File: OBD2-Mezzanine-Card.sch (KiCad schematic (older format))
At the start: 15 parts, among them P1 CONN_02X20

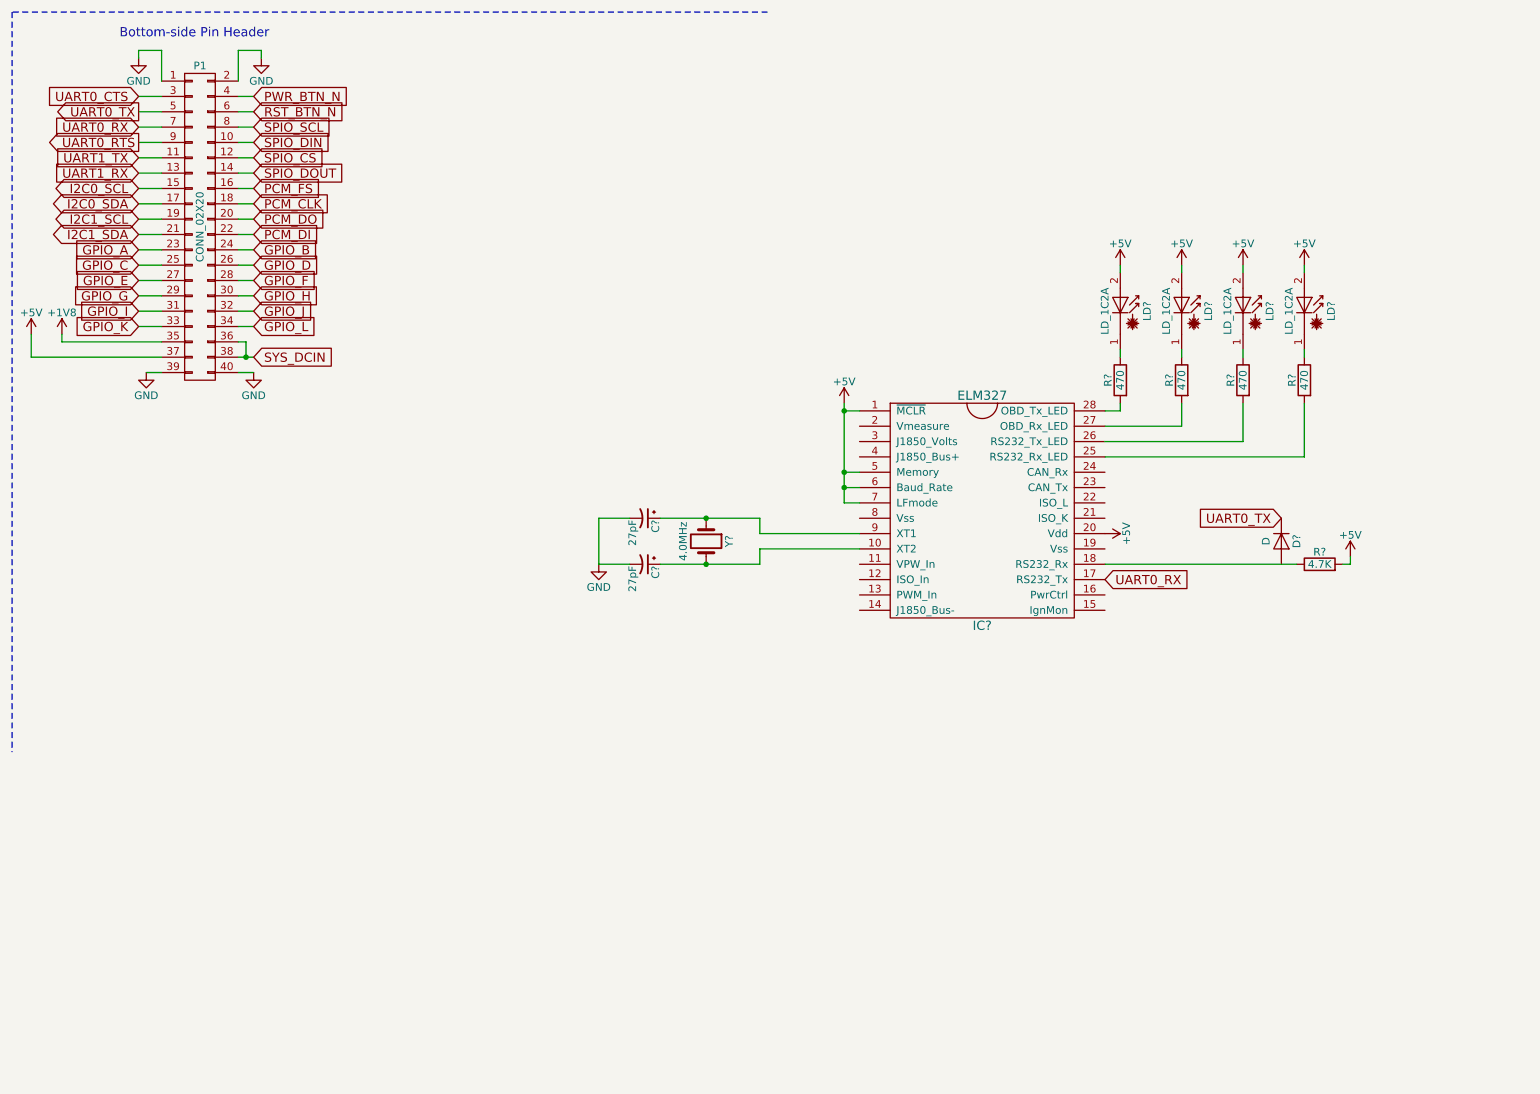
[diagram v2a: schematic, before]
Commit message: sch: Rearange
Signed-off-by: Alistair Francis <alistair@alistair23.me>
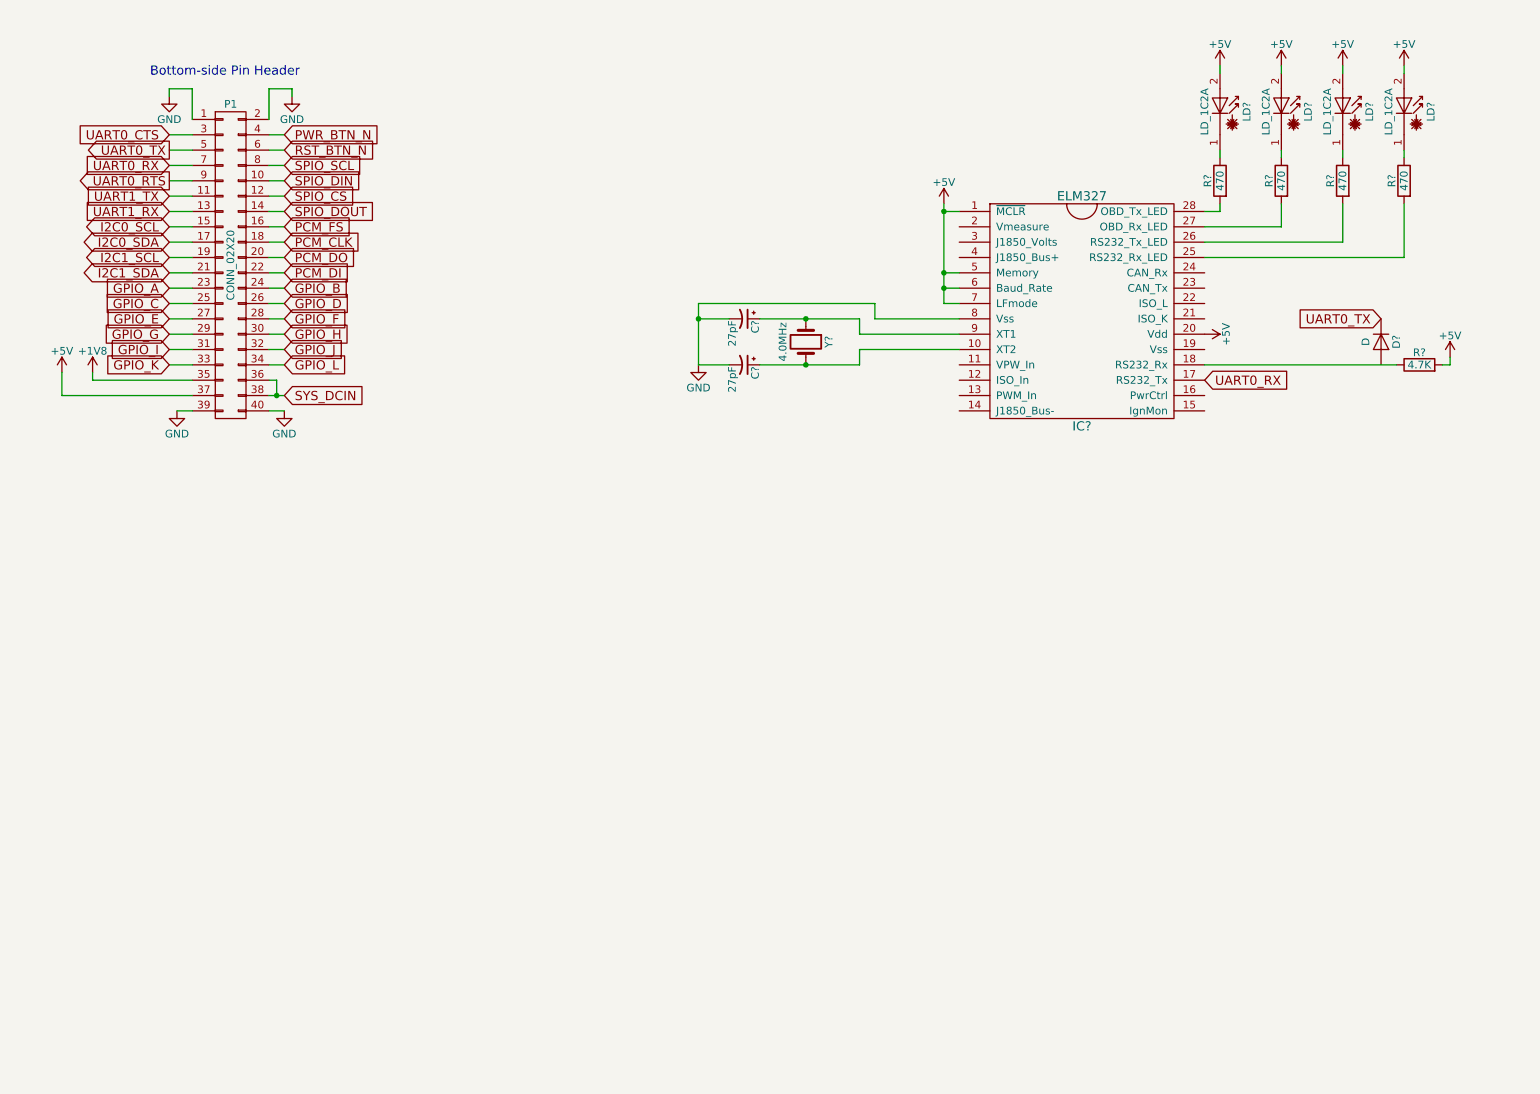
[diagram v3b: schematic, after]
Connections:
- net GND: now also IC?.8 (Vss)
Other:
- moved on the sheet: C?, D?, IC?, LD?, P1, R?, Y?

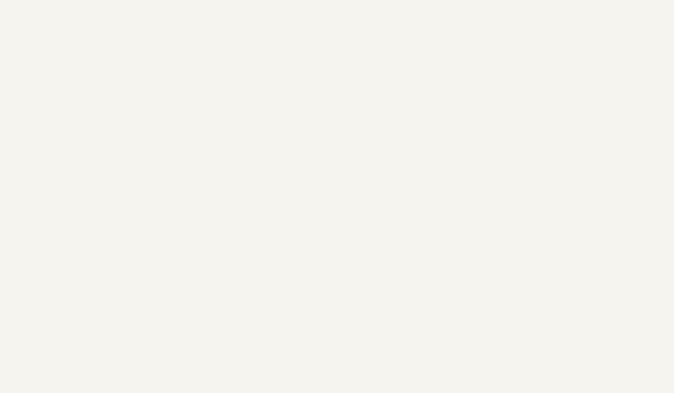
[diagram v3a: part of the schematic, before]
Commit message: sch: Add the MCP2561 CAN Transceiver
Signed-off-by: Alistair Francis <alistair@alistair23.me>
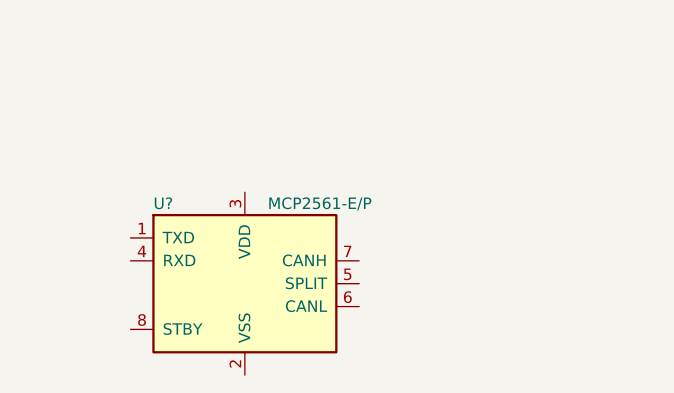
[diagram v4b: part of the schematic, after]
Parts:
- added U?: MCP2561-E/P, Housings_DIP:DIP-8_W7.62mm, symbol MCP2561-E/P
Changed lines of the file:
@@
 	6300 2550 5150 2550
 Connection ~ 5150 2650
+$Comp
+L MCP2561-E/P U?
+U 1 1 5AA61DC4
+P 1900 5700
+F 0 "U?" H 1500 6050 50  0000 L CNN
+F 1 "MCP2561-E/P" H 2000 6050 50  0000 L CNN
+F 2 "Housings_DIP:DIP-8_W7.62mm" H 1900 5200 50  0001 C CIN
+F 3 "" H 1900 5700 50  0001 C CNN
+	1    1900 5700
+	1    0    0    -1
+$EndComp
 $EndSCHEMATC

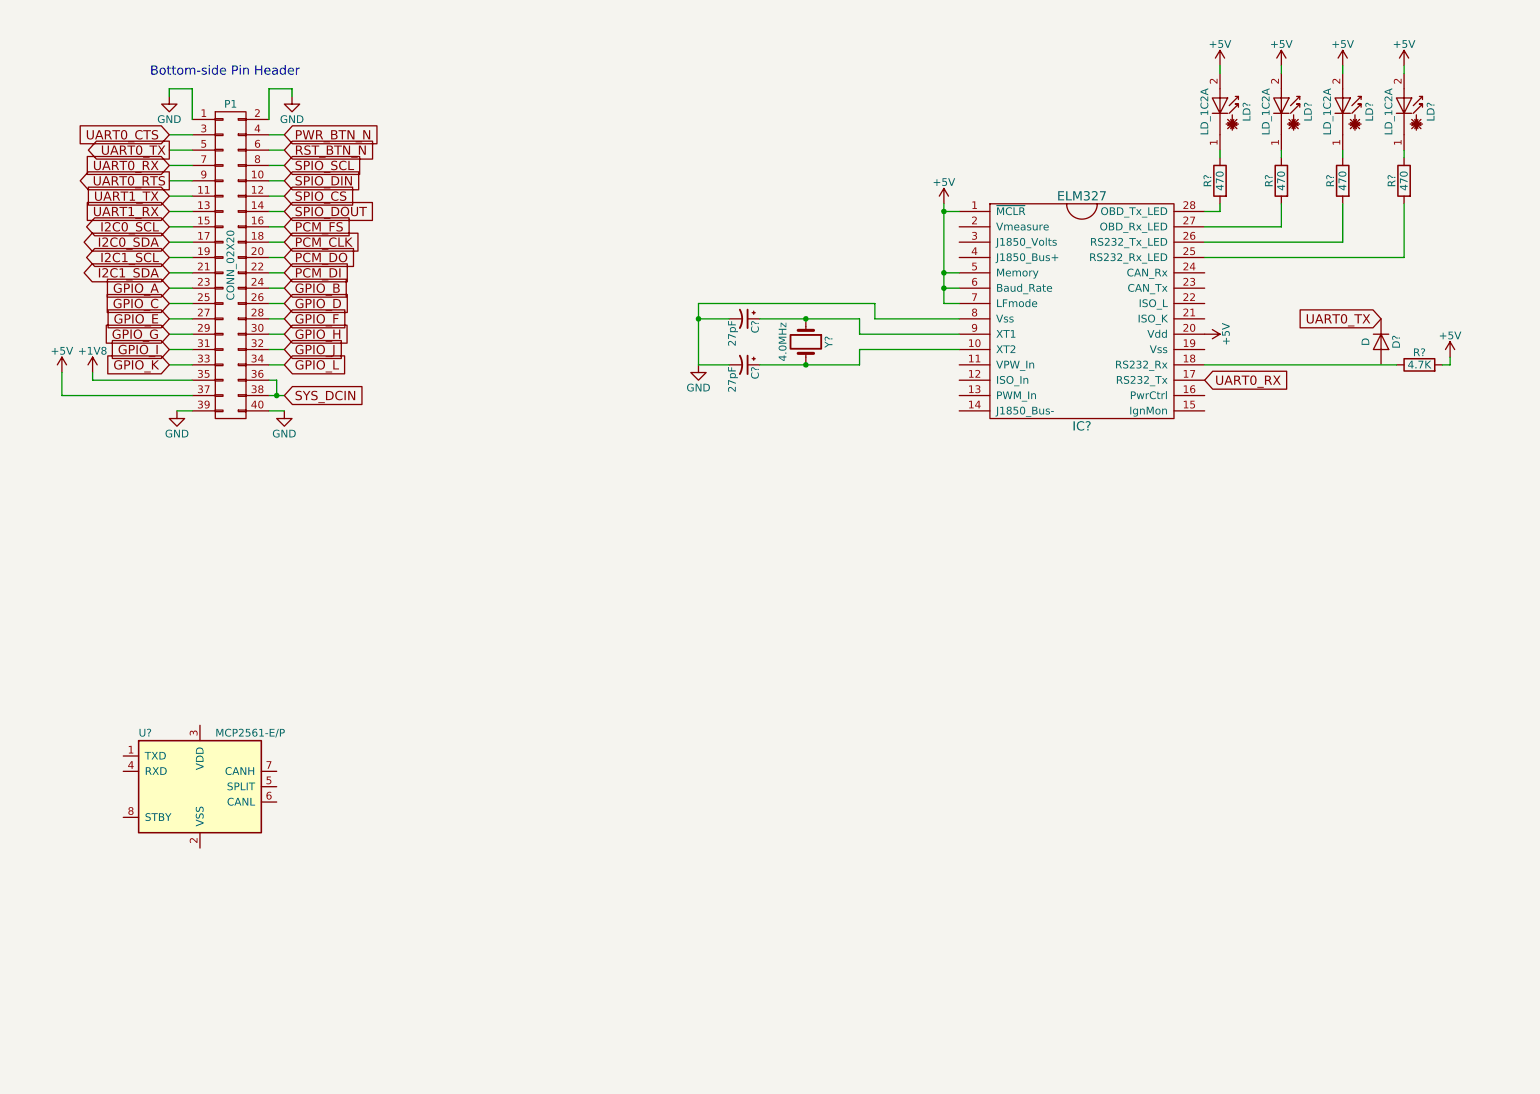
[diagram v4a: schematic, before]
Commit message: sch: Start to connect the CAN transceiver
Signed-off-by: Alistair Francis <alistair@alistair23.me>
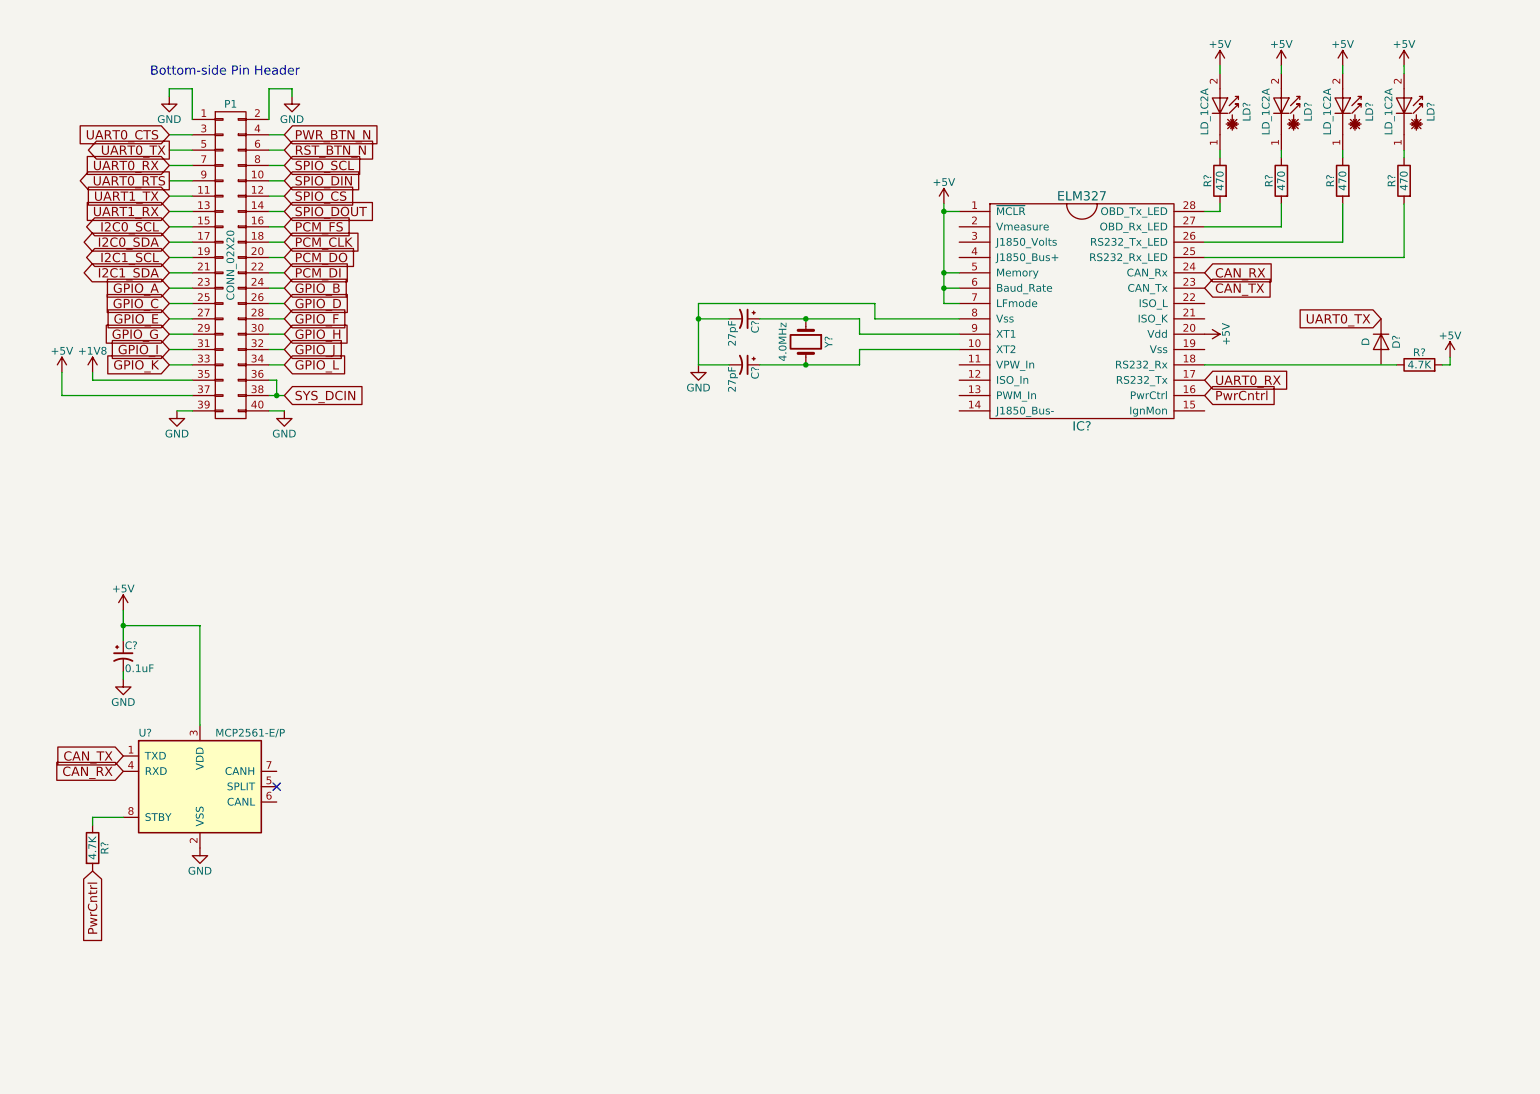
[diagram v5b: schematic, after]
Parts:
- added C?: 0.1uF, symbol CP1_Small
- added R?: 4.7K, symbol R
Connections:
- net +5V: now also U?.3 (VDD), C?.1
- net GND: now also U?.2 (VSS), C?.2
- net PwrCntrl: now reaches IC?.16 (PwrCtrl)
- net PwrCntrl: now also R?.2
- net CAN_TX: now reaches IC?.23 (CAN_Tx)
- net CAN_TX: now also U?.1 (TXD)
- net CAN_RX: now reaches IC?.24 (CAN_Rx)
- net CAN_RX: now also U?.4 (RXD)
- net at U?.8 (STBY): now also R?.1
- no-connect marks 0 -> 1
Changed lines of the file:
@@
 	1    0    0    -1
 $EndComp
+Text GLabel 1400 5600 0    60   Input ~ 0
+CAN_RX
+Text GLabel 8450 2350 2    60   Input ~ 0
+CAN_RX
+Text GLabel 8450 2450 2    60   Input ~ 0
+CAN_TX
+Text GLabel 1400 5500 0    60   Input ~ 0
+CAN_TX
+$Comp
+L GND #PWR?
+U 1 1 5AA5FF31
+P 1900 6100
+F 0 "#PWR?" H 1900 5850 50  0001 C CNN
+F 1 "GND" H 1900 5950 50  0000 C CNN
+F 2 "" H 1900 6100 50  0001 C CNN
+F 3 "" H 1900 6100 50  0001 C CNN
+	1    1900 6100
+	1    0    0    -1
+$EndComp
+$Comp
+L +5V #PWR?
+U 1 1 5AA5FFA4
+P 1400 4550
+F 0 "#PWR?" H 1400 4400 50  0001 C CNN
+F 1 "+5V" H 1400 4690 50  0000 C CNN
+F 2 "" H 1400 4550 50  0001 C CNN
+F 3 "" H 1400 4550 50  0001 C CNN
+	1    1400 4550
+	1    0    0    -1
+$EndComp
+$Comp
+L CP1_Small C?
+U 1 1 5AA5FFD8
+P 1400 4850
+F 0 "C?" H 1410 4920 50  0000 L CNN
+F 1 "0.1uF" H 1410 4770 50  0000 L CNN
+F 2 "" H 1400 4850 50  0001 C CNN
+F 3 "" H 1400 4850 50  0001 C CNN
+	1    1400 4850
+	1    0    0    -1
+$EndComp
+$Comp
+L GND #PWR?
+U 1 1 5AA600BE
+P 1400 5000
+F 0 "#PWR?" H 1400 4750 50  0001 C CNN
+F 1 "GND" H 1400 4850 50  0000 C CNN
+F 2 "" H 1400 5000 50  0001 C CNN
+F 3 "" H 1400 5000 50  0001 C CNN
+	1    1400 5000
+	1    0    0    -1
+$EndComp
+Wire Wire Line
+	1400 4550 1400 4750
+Wire Wire Line
+	1400 4950 1400 5000
+Wire Wire Line
+	1400 4650 1900 4650
+Wire Wire Line
+	1900 4650 1900 5300
+Connection ~ 1400 4650
+$Comp
+L R R?
+U 1 1 5AA6032D
+P 1200 6100
+F 0 "R?" V 1280 6100 50  0000 C CNN
+F 1 "4.7K" V 1200 6100 50  0000 C CNN
+F 2 "" V 1130 6100 50  0001 C CNN
+F 3 "" H 1200 6100 50  0001 C CNN
+	1    1200 6100
+	1    0    0    -1
+$EndComp
+Text GLabel 8450 3150 2    60   Input ~ 0
+PwrCntrl
+Text GLabel 1200 6250 3    60   Input ~ 0
+PwrCntrl
+Wire Wire Line
+	1400 5900 1200 5900
+Wire Wire Line
+	1200 5900 1200 5950
+NoConn ~ 2400 5700
 $EndSCHEMATC
